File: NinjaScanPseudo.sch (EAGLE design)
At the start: 57 parts, among them CON2 ZX62-B-5PA(11), CON3 JST_SH-12SM, IC1 LTC3550EDHC, IC2 MPU-6000, IC4 MAG3110FCR, J1 JUMPER1608, U1 DM3AT-SF-PEJM5, U2 H.FL, U3 NEO-6T, U4 MS5611-01BA01

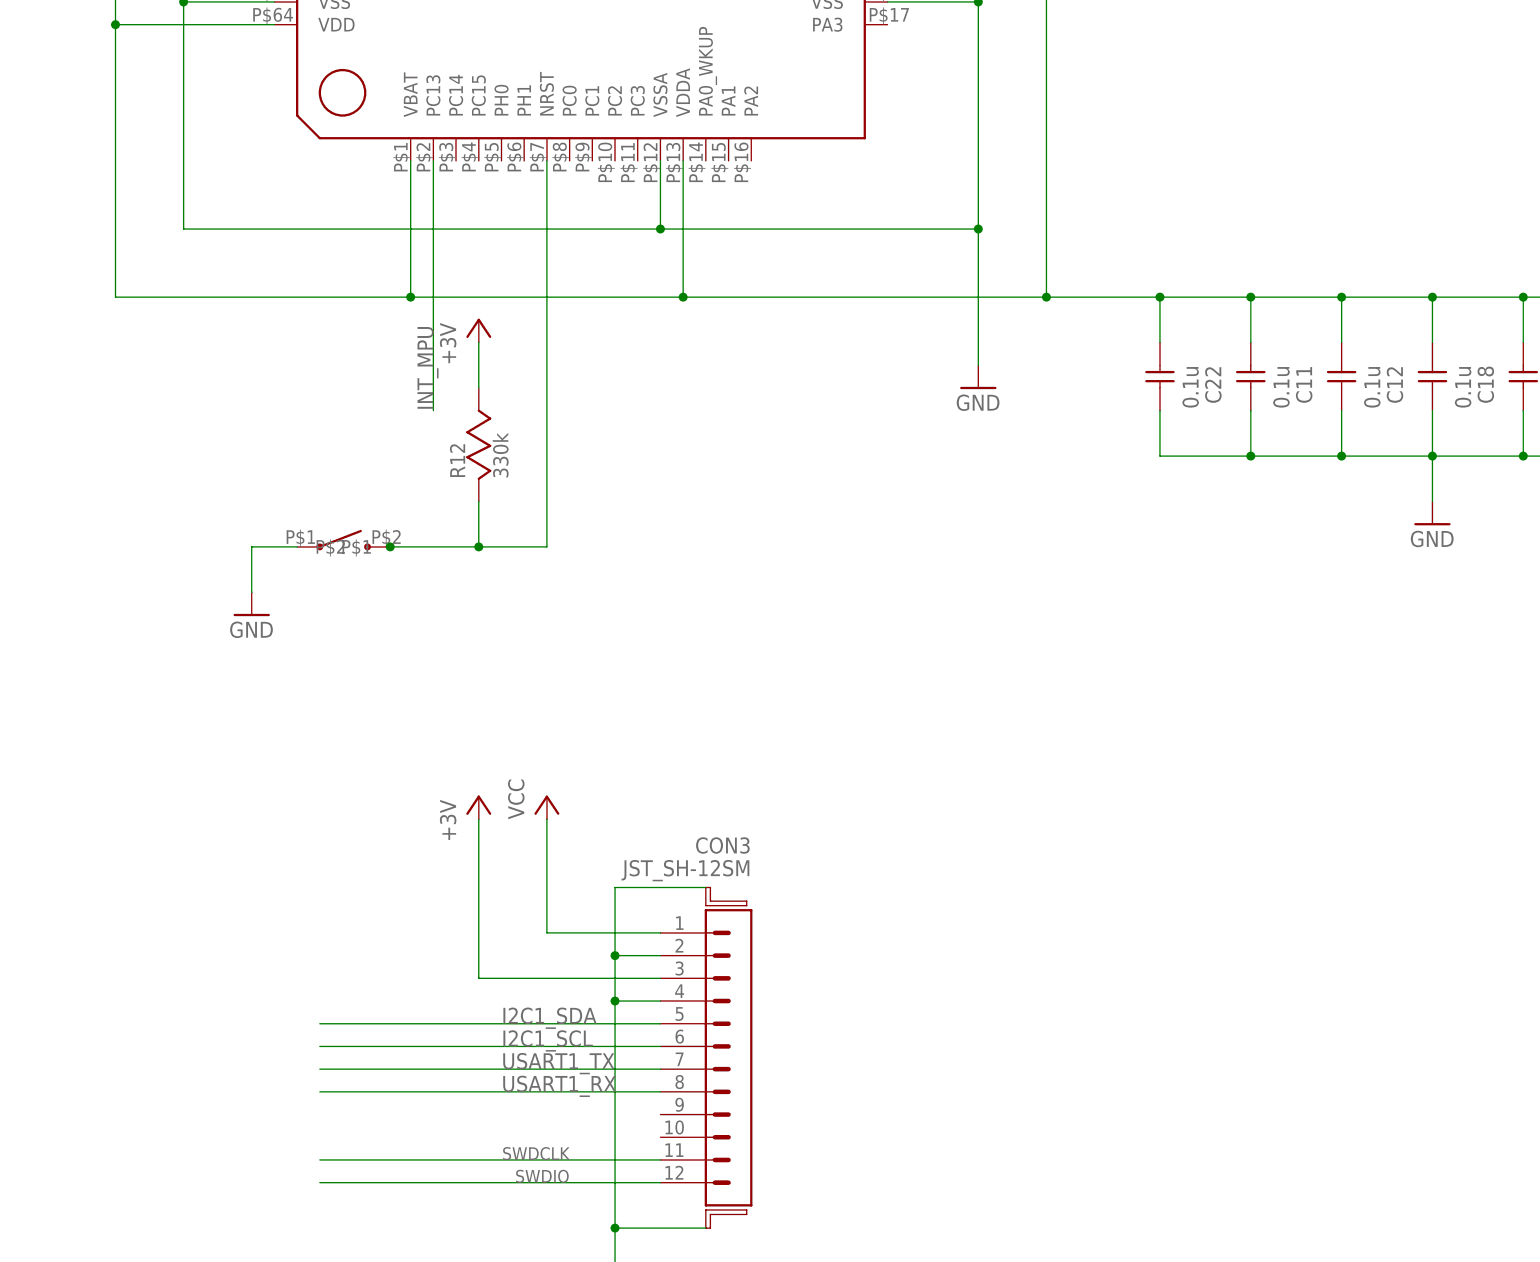
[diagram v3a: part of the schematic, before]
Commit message: XTAL added
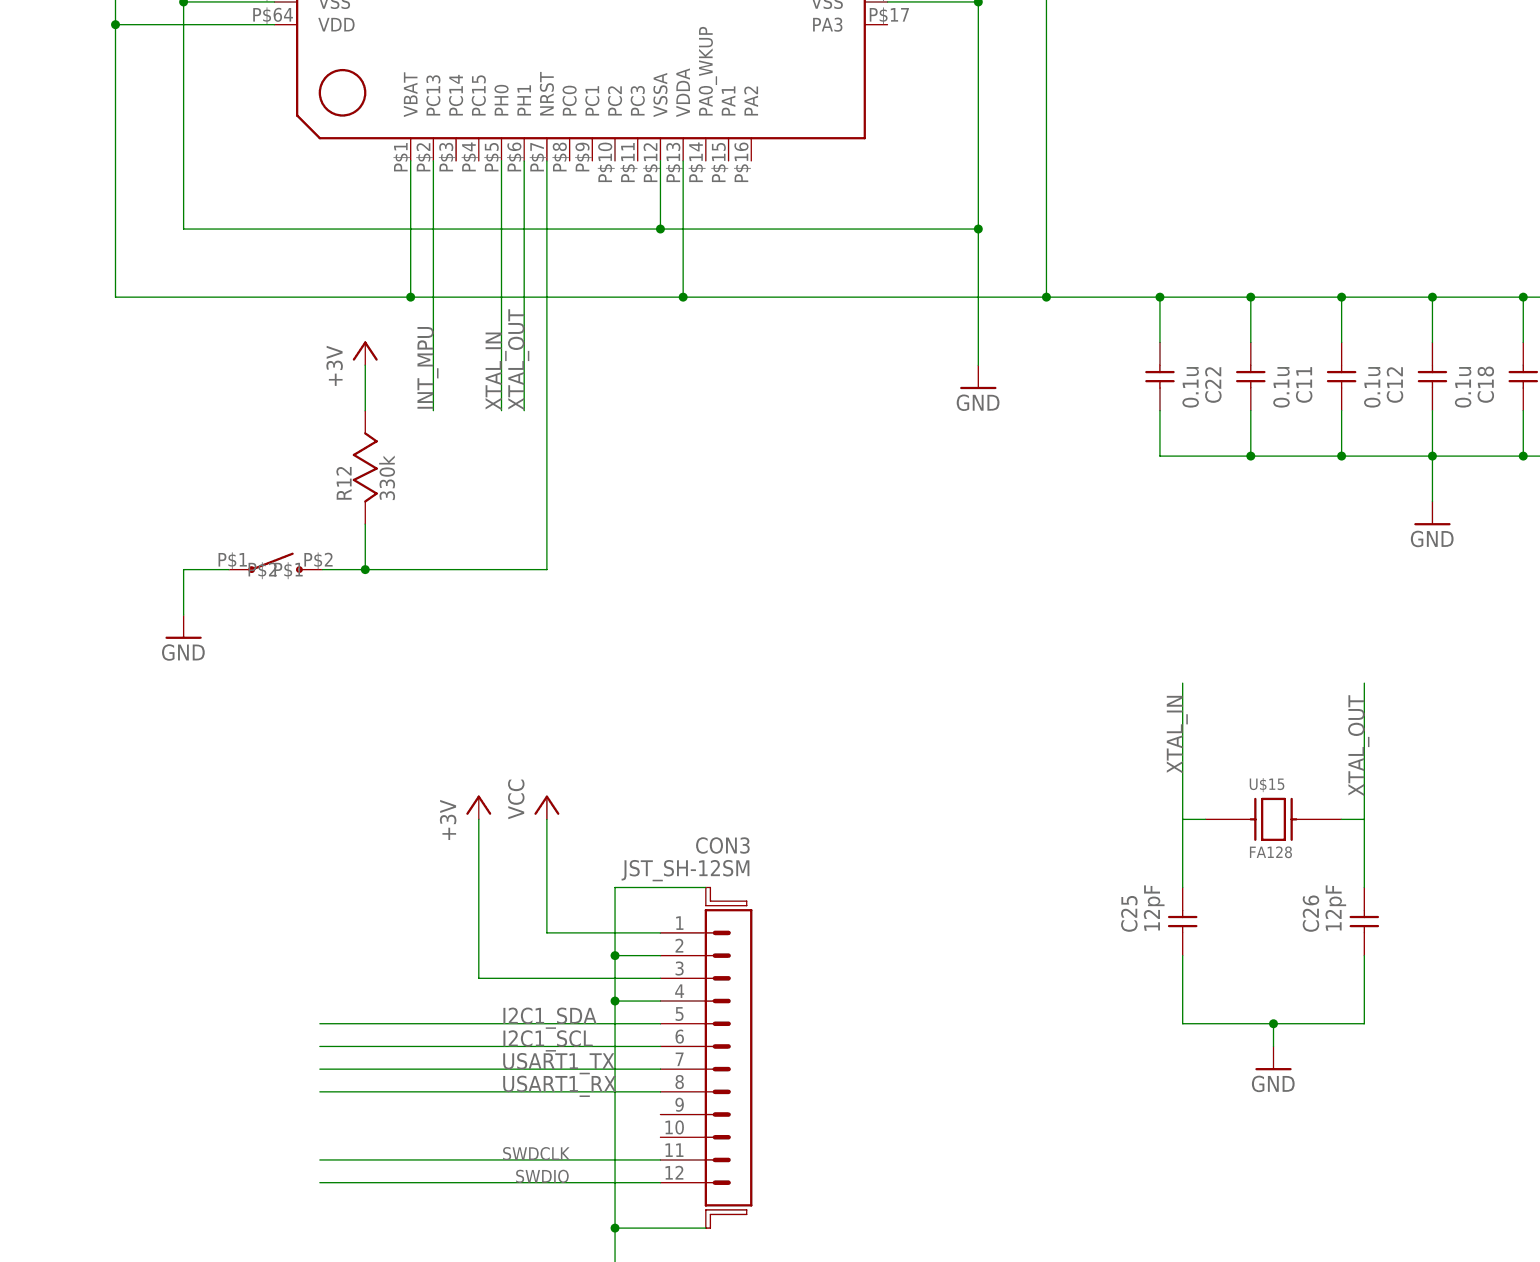
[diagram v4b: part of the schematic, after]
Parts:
- added C25, C26: 12pF, additional:C1005
- added U$15: FA128, mami_pero:FA128
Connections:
- new net XTAL_IN: C25.2, U$15.P$1, U$6.PH0
- new net XTAL_OUT: C26.2, U$15.P$2, U$6.PH1
- net GND: now also C25.1, C26.1
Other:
- note added: "GRM1555C1H120FA01D"
- note added: "Q22FA1280012000"
- moved on the sheet: R12
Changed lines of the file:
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@@
 <part name="C19" library="additional" deviceset="C" device="1005" value="0.1u"/>
 <part name="C24" library="additional" deviceset="C" device="1005" value="0.1u"/>
+<part name="U$15" library="mami_pero" deviceset="FA128" device=""/>
+<part name="C25" library="additional" deviceset="C" device="1005" value="12pF"/>
+<part name="C26" library="additional" deviceset="C" device="1005" value="12pF"/>
+<part name="GND11" library="supply1" deviceset="GND" device=""/>
 </parts>
 <sheets>
@@
 <text x="-104.14" y="-7.62" size="2.1844" layer="95" font="vector" ratio="15">IC2
 STM32F405RG</text>
+<text x="7.62" y="-177.8" size="1.778" layer="250">Q22FA1280012000</text>
+<text x="33.02" y="-182.88" size="1.778" layer="250">GRM1555C1H120FA01D</text>
 </plain>
 <instances>
@@
 <instance part="GND2" gate="1" x="-15.24" y="-121.92"/>
 <instance part="GND16" gate="1" x="35.56" y="-137.16"/>
-<instance part="GND9" gate="1" x="-96.52" y="-147.32"/>
-<instance part="U$8" gate="G$1" x="-88.9" y="-139.7"/>
+<instance part="GND9" gate="1" x="-104.14" y="-149.86"/>
+<instance part="U$8" gate="G$1" x="-96.52" y="-142.24"/>
 <instance part="LED3" gate="G$1" x="-40.64" y="20.32" rot="R270"/>
 <instance part="LED4" gate="G$1" x="-33.02" y="17.78" rot="R270"/>
@@
 <instance part="R14" gate="G$1" x="-33.02" y="-5.08" rot="R90"/>
 <instance part="U$11" gate="G$1" x="-111.76" y="0"/>
-<instance part="U$13" gate="G$1" x="-71.12" y="-114.3"/>
-<instance part="R12" gate="G$1" x="-71.12" y="-132.08" rot="R90"/>
+<instance part="U$13" gate="G$1" x="-83.82" y="-116.84"/>
+<instance part="R12" gate="G$1" x="-83.82" y="-134.62" rot="R90"/>
 <instance part="C23" gate="G$1" x="-2.54" y="-45.72" rot="R180"/>
 <instance part="C21" gate="G$1" x="-76.2" y="-17.78" rot="R270"/>
@@
 <instance part="C19" gate="G$1" x="45.72" y="-121.92" rot="R270"/>
 <instance part="C24" gate="G$1" x="55.88" y="-121.92" rot="R270"/>
+<instance part="U$15" gate="G$1" x="15.24" y="-170.18"/>
+<instance part="C25" gate="G$1" x="7.62" y="-180.34" rot="R90"/>
+<instance part="C26" gate="G$1" x="27.94" y="-180.34" rot="R90"/>
+<instance part="GND11" gate="1" x="17.78" y="-198.12"/>
 </instances>
 <busses>
@@
 <segment>
 <pinref part="GND9" gate="1" pin="GND"/>
-<wire x1="-96.52" y1="-139.7" x2="-96.52" y2="-144.78" width="0.1524" layer="91"/>
+<wire x1="-104.14" y1="-142.24" x2="-104.14" y2="-147.32" width="0.1524" layer="91"/>
 <pinref part="U$8" gate="G$1" pin="P$1"/>
-<wire x1="-96.52" y1="-139.7" x2="-91.44" y2="-139.7" width="0.1524" layer="91"/>
+<wire x1="-104.14" y1="-142.24" x2="-99.06" y2="-142.24" width="0.1524" layer="91"/>
+</segment>
+<segment>
+<pinref part="C25" gate="G$1" pin="1"/>
+<wire x1="7.62" y1="-185.42" x2="7.62" y2="-193.04" width="0.1524" layer="91"/>
+<pinref part="C26" gate="G$1" pin="1"/>
+<wire x1="7.62" y1="-193.04" x2="17.78" y2="-193.04" width="0.1524" layer="91"/>
+<wire x1="17.78" y1="-193.04" x2="27.94" y2="-193.04" width="0.1524" layer="91"/>
+<wire x1="27.94" y1="-193.04" x2="27.94" y2="-185.42" width="0.1524" layer="91"/>
+<pinref part="GND11" gate="1" pin="GND"/>
+<wire x1="17.78" y1="-195.58" x2="17.78" y2="-193.04" width="0.1524" layer="91"/>
+<junction x="17.78" y="-193.04"/>
 </segment>
 </net>
@@
 </segment>
 <segment>
-<wire x1="-71.12" y1="-116.84" x2="-71.12" y2="-121.92" width="0.1524" layer="91"/>
+<wire x1="-83.82" y1="-119.38" x2="-83.82" y2="-124.46" width="0.1524" layer="91"/>
 <pinref part="U$13" gate="G$1" pin="+3V"/>
 <pinref part="R12" gate="G$1" pin="2"/>
@@
 <segment>
 <pinref part="U$6" gate="G$1" pin="NRST"/>
-<wire x1="-63.5" y1="-96.52" x2="-63.5" y2="-139.7" width="0.1524" layer="91"/>
-<wire x1="-63.5" y1="-139.7" x2="-71.12" y2="-139.7" width="0.1524" layer="91"/>
-<wire x1="-71.12" y1="-134.62" x2="-71.12" y2="-139.7" width="0.1524" layer="91"/>
-<wire x1="-81.28" y1="-139.7" x2="-81.026" y2="-139.7" width="0.1524" layer="91"/>
-<junction x="-71.12" y="-139.7"/>
+<wire x1="-63.5" y1="-96.52" x2="-63.5" y2="-142.24" width="0.1524" layer="91"/>
+<wire x1="-63.5" y1="-142.24" x2="-83.82" y2="-142.24" width="0.1524" layer="91"/>
+<wire x1="-83.82" y1="-137.16" x2="-83.82" y2="-142.24" width="0.1524" layer="91"/>
+<junction x="-83.82" y="-142.24"/>
 <pinref part="U$8" gate="G$1" pin="P$2"/>
-<wire x1="-81.026" y1="-139.7" x2="-71.12" y2="-139.7" width="0.1524" layer="91"/>
-<junction x="-81.026" y="-139.7"/>
+<wire x1="-88.646" y1="-142.24" x2="-83.82" y2="-142.24" width="0.1524" layer="91"/>
 <pinref part="R12" gate="G$1" pin="1"/>
 </segment>
@@
 </segment>
 </net>
+<net name="XTAL_IN" class="0">
+<segment>
+<pinref part="U$6" gate="G$1" pin="PH0"/>
+<wire x1="-68.58" y1="-96.52" x2="-68.58" y2="-124.46" width="0.1524" layer="91"/>
+<label x="-68.58" y="-124.46" size="1.778" layer="95" rot="R90"/>
+</segment>
+<segment>
+<pinref part="U$15" gate="G$1" pin="P$1"/>
+<pinref part="C25" gate="G$1" pin="2"/>
+<wire x1="10.16" y1="-170.18" x2="7.62" y2="-170.18" width="0.1524" layer="91"/>
+<wire x1="7.62" y1="-170.18" x2="7.62" y2="-177.8" width="0.1524" layer="91"/>
+<wire x1="7.62" y1="-170.18" x2="7.62" y2="-154.94" width="0.1524" layer="91"/>
+<label x="7.62" y="-165.1" size="1.778" layer="95" rot="R90"/>
+</segment>
+</net>
+<net name="XTAL_OUT" class="0">
+<segment>
+<pinref part="U$6" gate="G$1" pin="PH1"/>
+<wire x1="-66.04" y1="-96.52" x2="-66.04" y2="-124.46" width="0.1524" layer="91"/>
+<label x="-66.04" y="-124.46" size="1.778" layer="95" rot="R90"/>
+</segment>
+<segment>
+<pinref part="U$15" gate="G$1" pin="P$2"/>
+<pinref part="C26" gate="G$1" pin="2"/>
+<wire x1="25.4" y1="-170.18" x2="27.94" y2="-170.18" width="0.1524" layer="91"/>
+<wire x1="27.94" y1="-170.18" x2="27.94" y2="-177.8" width="0.1524" layer="91"/>
+<wire x1="27.94" y1="-170.18" x2="27.94" y2="-154.94" width="0.1524" layer="91"/>
+<label x="27.94" y="-167.64" size="1.778" layer="95" rot="R90"/>
+</segment>
+</net>
